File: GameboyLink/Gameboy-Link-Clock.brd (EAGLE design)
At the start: 67.6 x 39 mm, 37 parts, among them IC1 MEGA8-AI, J1 AVR_SPI_PRG_6PTH, Q1 16MHz, U1 DS1307Z, Y1 32.768kHz

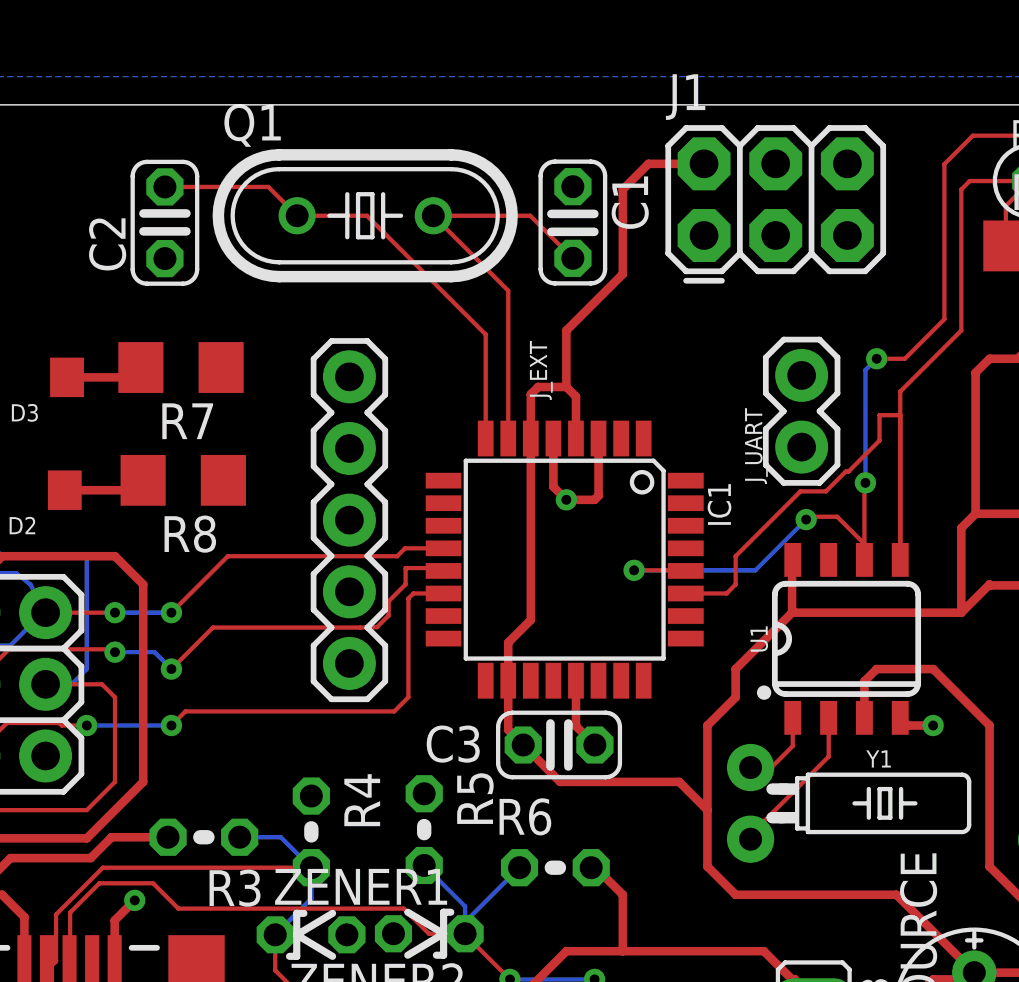
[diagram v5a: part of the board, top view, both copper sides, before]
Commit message: Routing done draft!  Need to add ADC channels
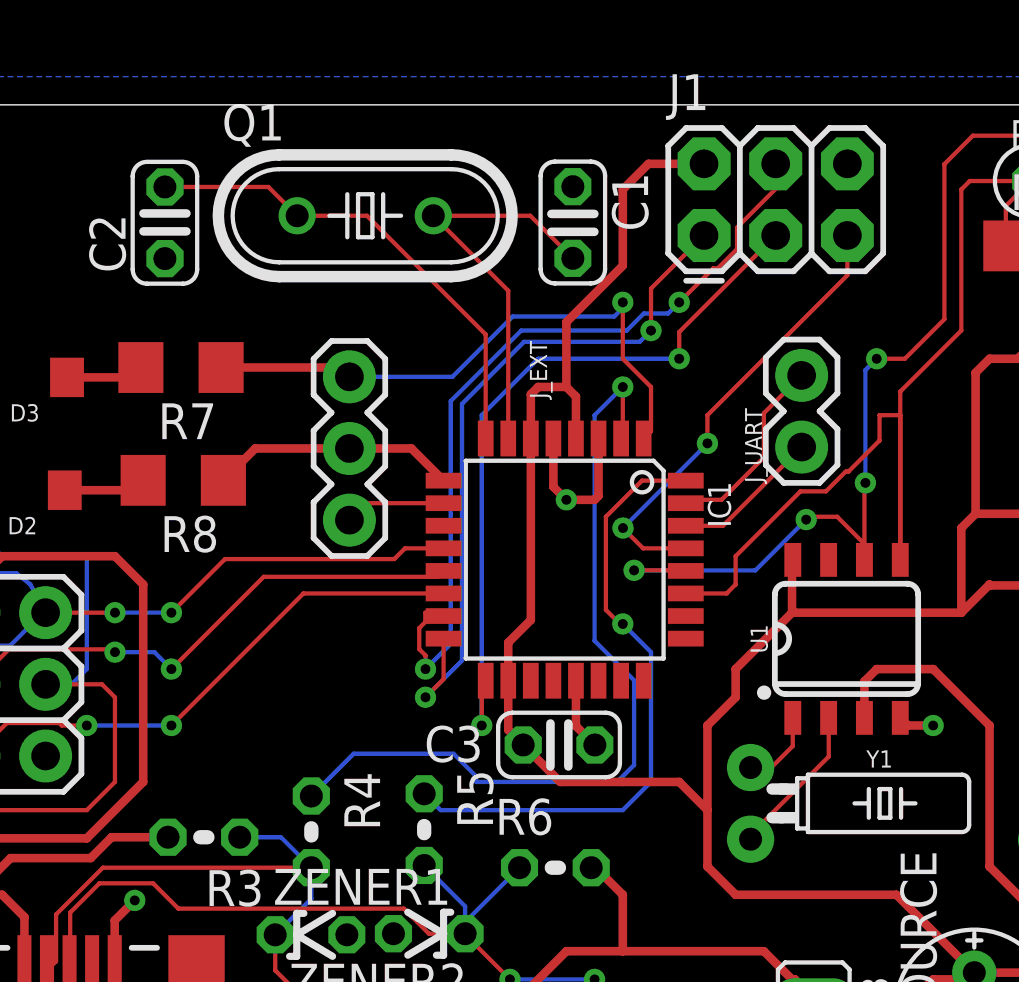
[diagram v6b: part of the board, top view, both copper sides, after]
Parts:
- J_EXT: value (none) -> 455-1750-1-ND; device SparkFun-Connectors:1X05 -> SparkFun-Connectors:1X03
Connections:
- removed net N$10: IC1.9, J_EXT.2
- removed net N$21: IC1.19, R8.1
- removed net N$22: IC1.22, R7.1
- removed net N$6: IC1.1, J_EXT.1
- new net N$17: IC1.9, J_EXT.2, R8.1
- new net N$9: IC1.1, J_EXT.1, R7.1
- net N$15: no longer J_EXT.5
- net N$18: no longer J_EXT.4
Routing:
- net D-: track 0.00 -> 29.1 mm, vias 0 -> 1
- net N$7: track 0.00 -> 28.7 mm, vias 0 -> 2
- net N$3: track 0.00 -> 26.3 mm, vias 0 -> 2
- net N$8: track 0.00 -> 25.2 mm, vias 0 -> 2
- net D+: track 0.00 -> 22.2 mm, vias 0 -> 1
- net N$9: track 0.00 -> 20.9 mm, vias 0 -> 1
- net RESET: track 0.00 -> 16.2 mm, vias 0 -> 2
- net N$17: track 0.00 -> 8.75 mm
- net N$13: track 0.00 -> 6.90 mm
- net N$12: track 0.00 -> 5.26 mm
- net N$11: track 0.00 -> 3.59 mm
- net GB_CLK: track 53.1 -> 51.1 mm
- net GB_MISO: track 54.2 -> 53.6 mm

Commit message: All routed, now cosmetics and indepth review.
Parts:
- added J_ADC: (no value), SparkFun-Connectors:1X02
- moved Y1 1.00 mm to (51.5, 13.2)
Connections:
- net N$15: now also J_ADC.2
- net N$18: now also J_ADC.1
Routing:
- net D-: track 29.1 -> 23.9 mm
- net N$18: track 0.00 -> 5.21 mm
- net D+: track 22.2 -> 18.6 mm
- net N$15: track 0.00 -> 2.46 mm
- net VCC: track 111.3 -> 112.2 mm
- net N$23: track 2.81 -> 2.25 mm

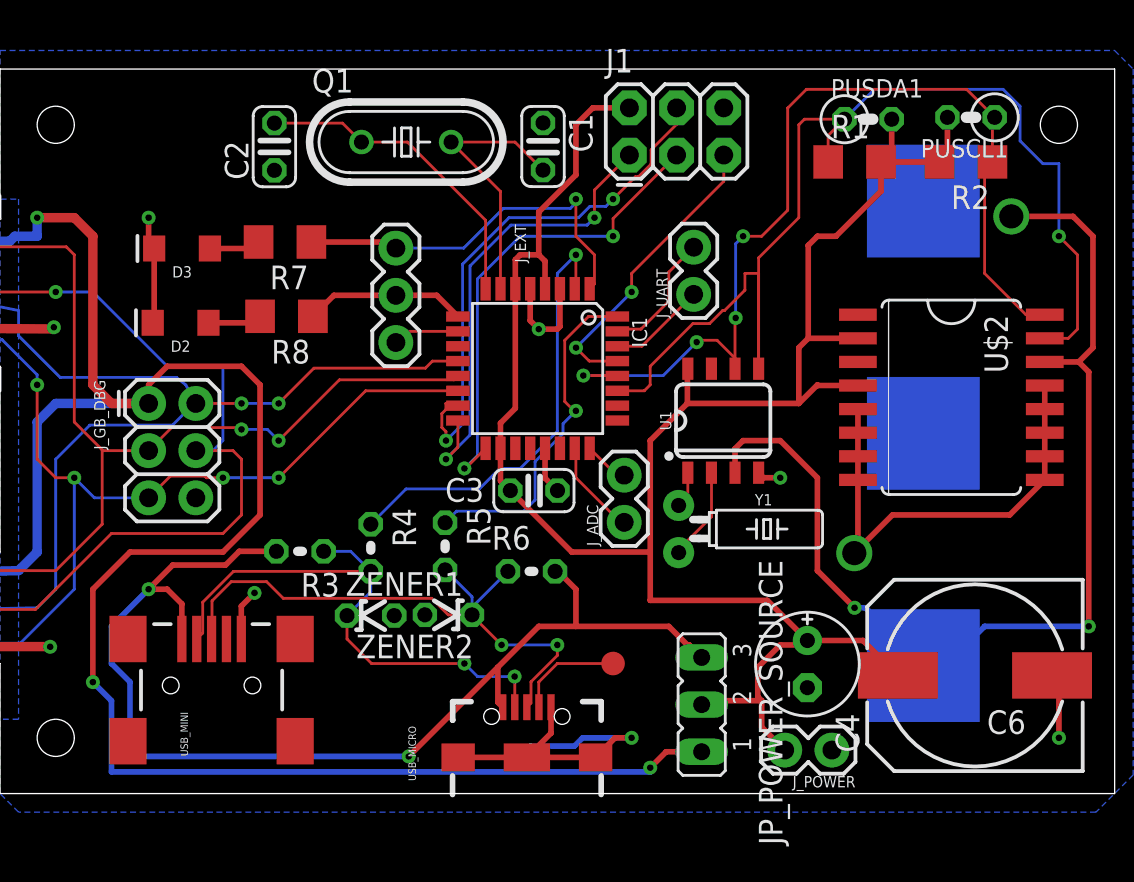
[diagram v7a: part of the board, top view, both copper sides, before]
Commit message: Overall layout ok first pass, now cosmetics
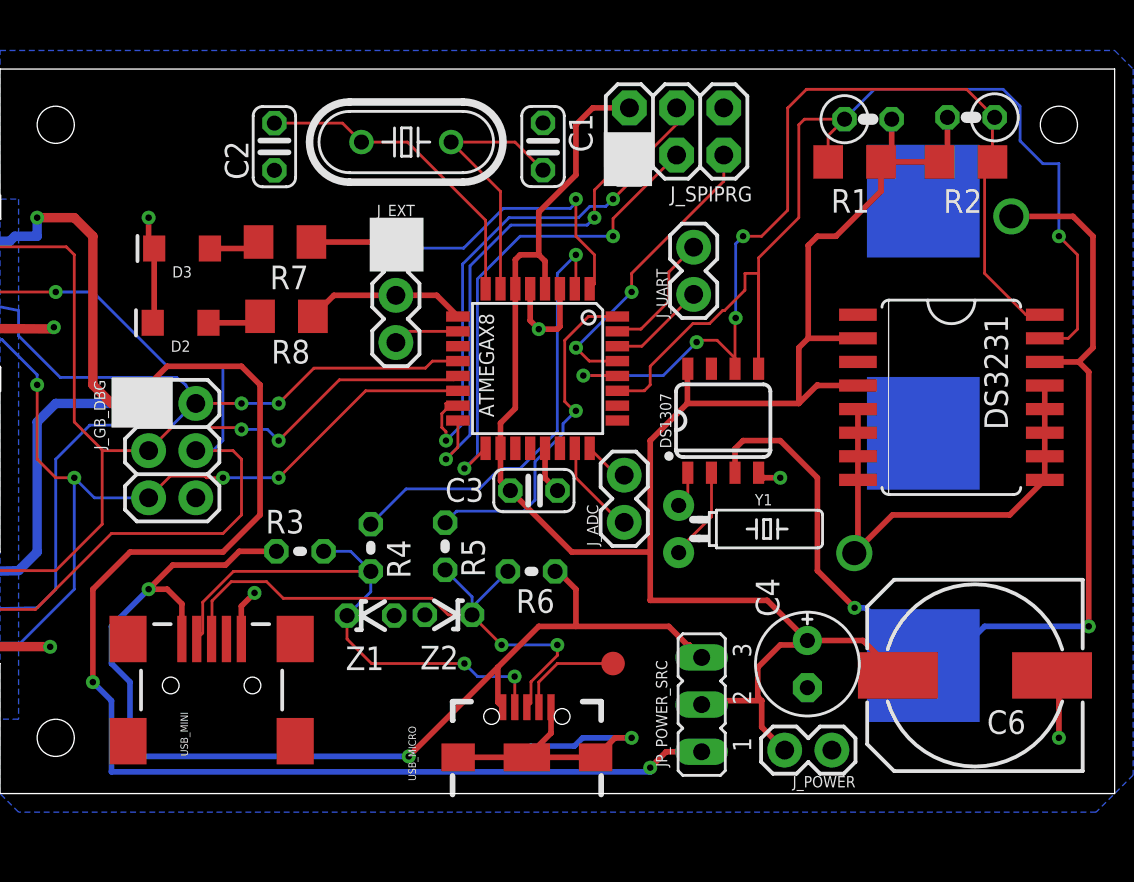
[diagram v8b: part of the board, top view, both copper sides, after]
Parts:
- renumbered IC1 to ATMEGAX8, J1 to J_SPIPRG, JP_POWER_SOURCE to JP_POWER_SRC, U$2 to DS3231, U1 to DS1307, ZENER1 to Z1, ZENER2 to Z2
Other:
- board text added: "+"
- board text added: "-"
- board text added: "GBA/GBC"
- board text added: "GBO"
